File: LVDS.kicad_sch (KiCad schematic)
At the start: 16 parts, among them J13 DF13C-3P-1.25V_21_, J3 QSH-030-01-X-D-A-XX, U10 TCAN1042HVDQ1, U11 SN74AVC2T245_UQFN

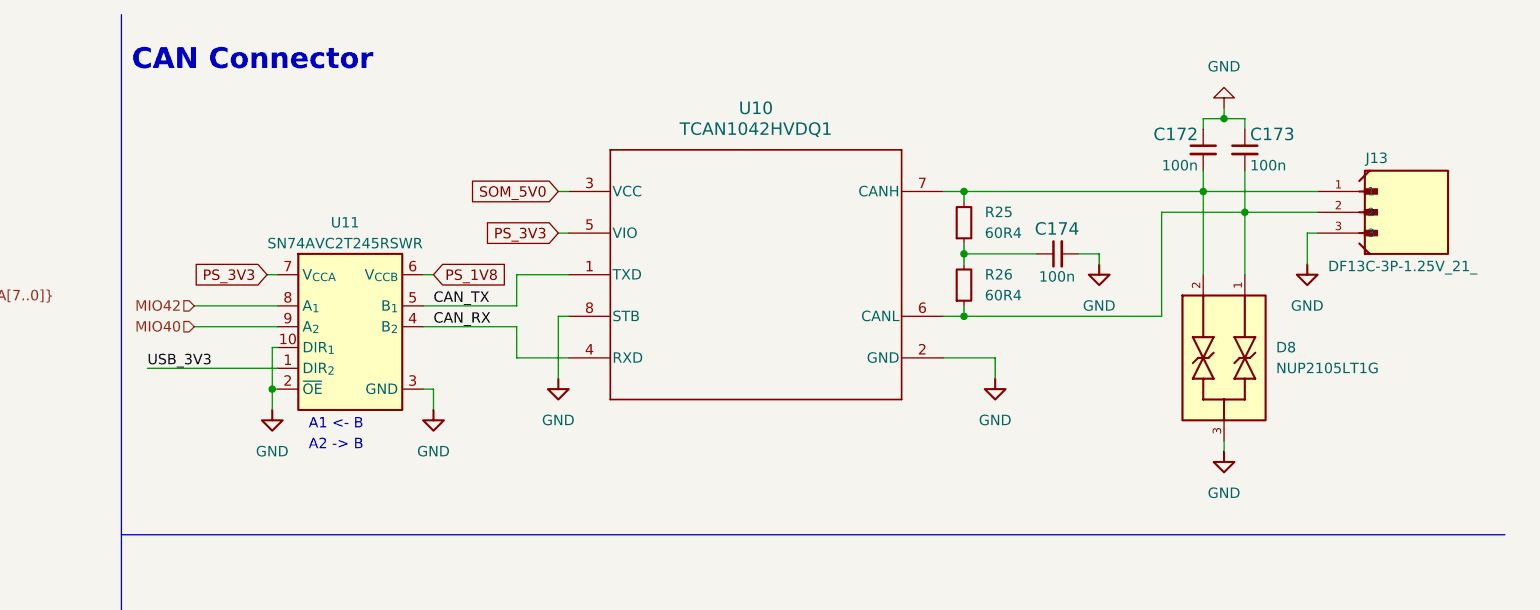
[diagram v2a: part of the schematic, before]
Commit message: Routed CAN portion of board
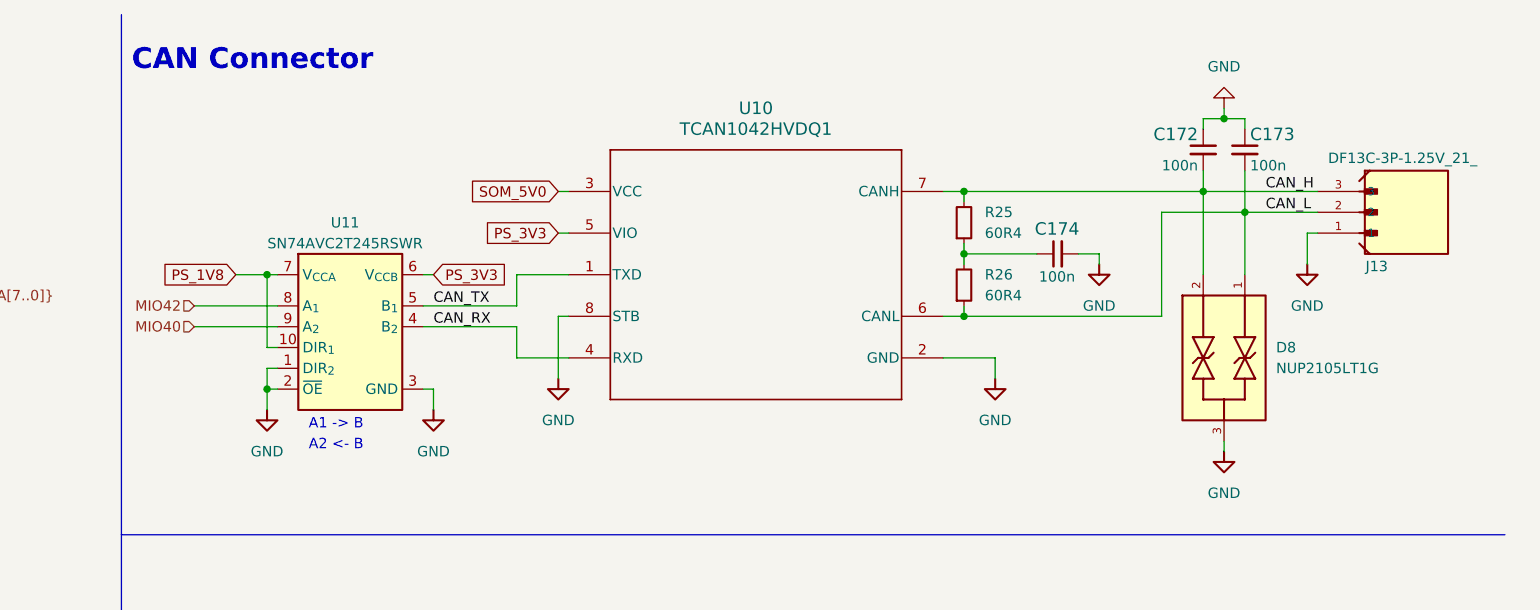
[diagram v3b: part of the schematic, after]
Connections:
- net USB_3V3 is gone; now on net GND: U11.1 (DIR_{2})
- net GND: now also J13.1; no longer J13.3, U11.10 (DIR_{1})
- net PS_1V8: now also U11.10 (DIR_{1}), U11.7 (V_{CCA}); no longer U11.6 (V_{CCB})
- net PS_3V3: now also U11.6 (V_{CCB}); no longer U11.7 (V_{CCA})
- net CAN_H: now reaches C172.2, D8.2, R25.2, U10.7 (CANH)
- net CAN_H: now also J13.3; no longer J13.1
- net CAN_L: now reaches C173.2, D8.1, J13.2, R26.1, U10.6 (CANL)
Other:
- note added: "A1 -> B"
- note added: "A2 <- B"
- note removed: "A1 <- B"
- note removed: "A2 -> B"
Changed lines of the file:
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@@
 		)
 	)
-	(text "A2 -> B"
+	(text "A2 <- B"
 		(exclude_from_sim no)
 		(at 138.43 66.04 0)
@@
 		)
 	)
-	(text "A1 <- B"
+	(text "A1 -> B"
 		(exclude_from_sim no)
 		(at 138.43 63.5 0)
@@
 	)
 	(junction
-		(at 218.44 41.91)
+		(at 133.35 44.45)
 		(diameter 0)
 		(color 0 0 0 0)
 	)
 	(junction
-		(at 54.61 55.88)
+		(at 218.44 41.91)
 		(diameter 0)
 		(color 0 0 0 0)
 	)
 	(junction
-		(at 218.44 34.29)
+		(at 54.61 55.88)
 		(diameter 0)
 		(color 0 0 0 0)
 	)
 	(junction
-		(at 133.985 58.42)
+		(at 218.44 34.29)
 		(diameter 0)
 		(color 0 0 0 0)
@@
 	)
 	(junction
+		(at 133.35 58.42)
+		(diameter 0)
+		(color 0 0 0 0)
+	)
+	(junction
 		(at 54.61 109.22)
 		(diameter 0)
@@
 	(wire
 		(pts
-			(xy 133.985 58.42) (xy 134.62 58.42)
+			(xy 133.35 58.42) (xy 134.62 58.42)
 		)
 		(stroke
@@
 	(wire
 		(pts
+			(xy 133.35 44.45) (xy 134.62 44.45)
+		)
+		(stroke
+			(width 0)
+			(type default)
+		)
+	)
+	(wire
+		(pts
 			(xy 152.4 44.45) (xy 153.67 44.45)
 		)
@@
 	(wire
 		(pts
-			(xy 53.34 55.88) (xy 54.61 55.88)
+			(xy 133.35 55.88) (xy 134.62 55.88)
 		)
 		(stroke
@@
 	(wire
 		(pts
-			(xy 234.95 43.18) (xy 234.95 41.91)
+			(xy 129.54 44.45) (xy 133.35 44.45)
 		)
 		(stroke
@@
 	(wire
 		(pts
-			(xy 168.91 39.37) (xy 170.18 39.37)
+			(xy 53.34 55.88) (xy 54.61 55.88)
 		)
 		(stroke
@@
 	(wire
 		(pts
-			(xy 54.61 71.12) (xy 54.61 78.74)
+			(xy 234.95 43.18) (xy 234.95 41.91)
 		)
 		(stroke
@@
 	(wire
 		(pts
-			(xy 53.34 58.42) (xy 91.44 58.42)
+			(xy 168.91 39.37) (xy 170.18 39.37)
 		)
 		(stroke
@@
 	(wire
 		(pts
-			(xy 134.62 53.34) (xy 133.985 53.34)
+			(xy 54.61 71.12) (xy 54.61 78.74)
+		)
+		(stroke
+			(width 0)
+			(type default)
+		)
+	)
+	(wire
+		(pts
+			(xy 53.34 58.42) (xy 91.44 58.42)
 		)
 		(stroke
@@
 	(wire
 		(pts
-			(xy 133.985 58.42) (xy 133.985 60.96)
+			(xy 133.35 58.42) (xy 133.35 60.96)
 		)
 		(stroke
@@
 	(wire
 		(pts
-			(xy 24.13 147.32) (xy 24.13 148.59)
+			(xy 133.35 55.88) (xy 133.35 58.42)
 		)
 		(stroke
@@
 	(wire
 		(pts
-			(xy 133.35 44.45) (xy 134.62 44.45)
+			(xy 24.13 147.32) (xy 24.13 148.59)
 		)
 		(stroke
@@
 	(wire
 		(pts
+			(xy 133.35 44.45) (xy 133.35 53.34)
+		)
+		(stroke
+			(width 0)
+			(type default)
+		)
+	)
+	(wire
+		(pts
 			(xy 168.91 49.53) (xy 168.91 57.15)
 		)
@@
 	(wire
 		(pts
-			(xy 134.62 55.88) (xy 118.745 55.88)
+			(xy 53.34 88.9) (xy 91.44 88.9)
 		)
 		(stroke
@@
 	(wire
 		(pts
-			(xy 53.34 88.9) (xy 91.44 88.9)
+			(xy 218.44 48.26) (xy 218.44 49.53)
 		)
 		(stroke
@@
 	(wire
 		(pts
-			(xy 218.44 48.26) (xy 218.44 49.53)
+			(xy 53.34 96.52) (xy 91.44 96.52)
 		)
 		(stroke
@@
 	(wire
 		(pts
-			(xy 53.34 96.52) (xy 91.44 96.52)
+			(xy 53.34 86.36) (xy 54.61 86.36)
 		)
 		(stroke
@@
 	(wire
 		(pts
-			(xy 53.34 86.36) (xy 54.61 86.36)
+			(xy 124.46 48.26) (xy 134.62 48.26)
 		)
 		(stroke
@@
 	(wire
 		(pts
-			(xy 124.46 48.26) (xy 134.62 48.26)
+			(xy 54.61 101.6) (xy 54.61 106.68)
 		)
 		(stroke
@@
 	(wire
 		(pts
-			(xy 54.61 101.6) (xy 54.61 106.68)
+			(xy 53.34 48.26) (xy 54.61 48.26)
 		)
 		(stroke
@@
 	(wire
 		(pts
-			(xy 53.34 48.26) (xy 54.61 48.26)
+			(xy 133.35 53.34) (xy 134.62 53.34)
 		)
 		(stroke
@@
 	(wire
 		(pts
-			(xy 133.985 53.34) (xy 133.985 58.42)
-		)
-		(stroke
-			(width 0)
-			(type default)
-		)
-	)
-	(wire
-		(pts
 			(xy 168.91 34.29) (xy 170.18 34.29)
 		)
@@
 		)
 	)
+	(label "CAN_L"
+		(at 255.27 36.83 0)
+		(effects
+			(font
+				(size 1.27 1.27)
+			)
+			(justify left bottom)
+		)
+	)
 	(label "HPA02_N"
 		(at 90.17 91.44 180)
@@
 		)
 	)
+	(label "CAN_H"
+		(at 255.27 34.29 0)
+		(effects
+			(font
+				(size 1.27 1.27)
+			)
+			(justify left bottom)
+		)
+	)
 	(label "HPA02_P"
 		(at 90.17 88.9 180)
@@
 		)
 	)
-	(label "USB_3V3"
-		(at 118.745 55.88 0)
-		(effects
-			(font
-				(size 1.27 1.27)
-			)
-			(justify left bottom)
-		)
-	)
 	(label "LVDS_2P"
 		(at 68.58 73.66 180)
@@
 	(global_label "PS_1V8"
 		(shape input)
-		(at 153.67 44.45 0)
+		(at 129.54 44.45 180)
 		(fields_autoplaced yes)
 		(effects
@@
 				(size 1.27 1.27)
 			)
-			(justify left)
+			(justify right)
 		)
 		(property "Intersheetrefs" "${INTERSHEET_REFS}"
-			(at 162.949 44.3706 0)
+			(at 120.261 44.3706 0)
 			(effects
 				(font
 					(size 1.27 1.27)
 				)
-				(justify left)
+				(justify right)
 				(hide yes)
 			)
@@
 	(global_label "PS_3V3"
 		(shape input)
-		(at 133.35 44.45 180)
+		(at 153.67 44.45 0)
 		(fields_autoplaced yes)
 		(effects
@@
 				(size 1.27 1.27)
 			)
-			(justify right)
+			(justify left)
 		)
 		(property "Intersheetrefs" "${INTERSHEET_REFS}"
-			(at 101.6 -204.47 0)
+			(at 185.42 -204.47 0)
 			(effects
 				(font
 					(size 1.27 1.27)
 				)
-				(justify left)
+				(justify right)
 				(hide yes)
 			)
@@
 		(lib_id "kria-k26-devboard:DF13C-3P-1.25V_21_")
 		(at 271.78 36.83 0)
+		(mirror x)
 		(unit 1)
 		(exclude_from_sim no)
@@
 		(dnp no)
 		(property "Reference" "J13"
-			(at 267.462 30.226 0)
+			(at 267.462 43.434 0)
 			(effects
 				(font
@@
 		)
 		(property "Value" "DF13C-3P-1.25V_21_"
-			(at 262.89 43.434 0)
+			(at 262.89 30.226 0)
 			(effects
 				(font
@@
 	(symbol
 		(lib_id "kria-k26-devboard:GND")
-		(at 133.985 60.96 0)
+		(at 133.35 60.96 0)
 		(unit 1)
 		(exclude_from_sim no)
@@
 		(fields_autoplaced yes)
 		(property "Reference" "#PWR018"
-			(at 133.985 67.31 0)
+			(at 133.35 67.31 0)
 			(effects
 				(font
@@
 		)
 		(property "Value" "GND"
-			(at 133.985 66.04 0)
+			(at 133.35 66.04 0)
 			(effects
 				(font
@@
 		)
 		(property "Footprint" ""
-			(at 142.875 68.58 0)
+			(at 142.24 68.58 0)
 			(effects
 				(font
@@
 		)
 		(property "Datasheet" ""
-			(at 142.875 73.66 0)
+			(at 142.24 73.66 0)
 			(effects
 				(font
@@
 		)
 		(property "Description" ""
-			(at 133.985 60.96 0)
+			(at 133.35 60.96 0)
 			(effects
 				(font
@@
 		)
 		(property "Author" "Antmicro"
-			(at 142.875 68.58 0)
+			(at 142.24 68.58 0)
 			(effects
 				(font
@@
 		)
 		(property "License" "Apache-2.0"
-			(at 142.875 71.12 0)
+			(at 142.24 71.12 0)
 			(effects
 				(font

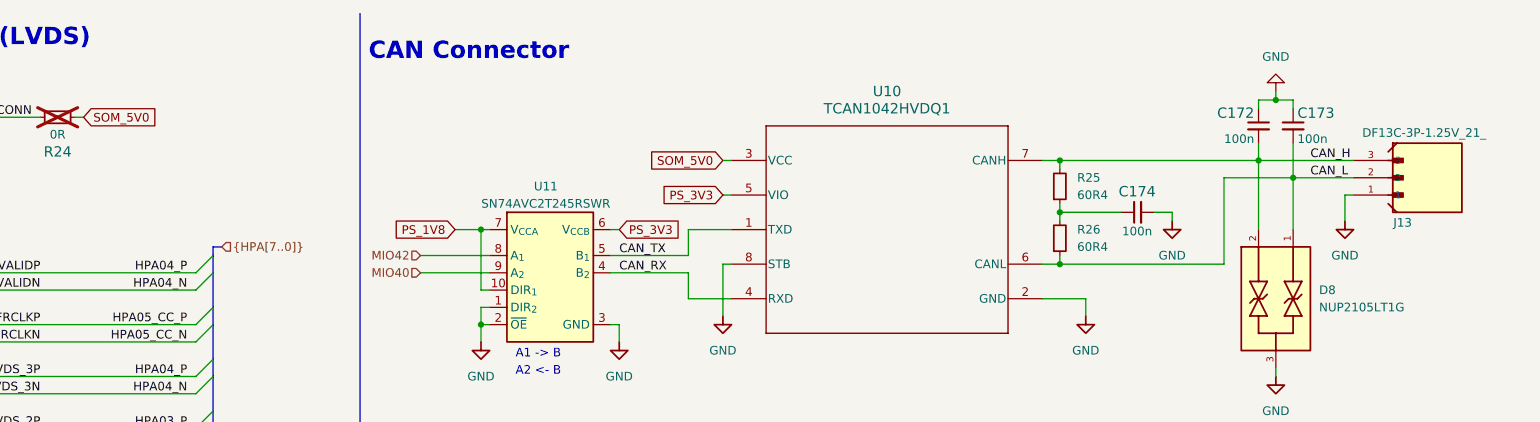
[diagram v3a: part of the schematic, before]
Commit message: Finished first set of LVDS signals
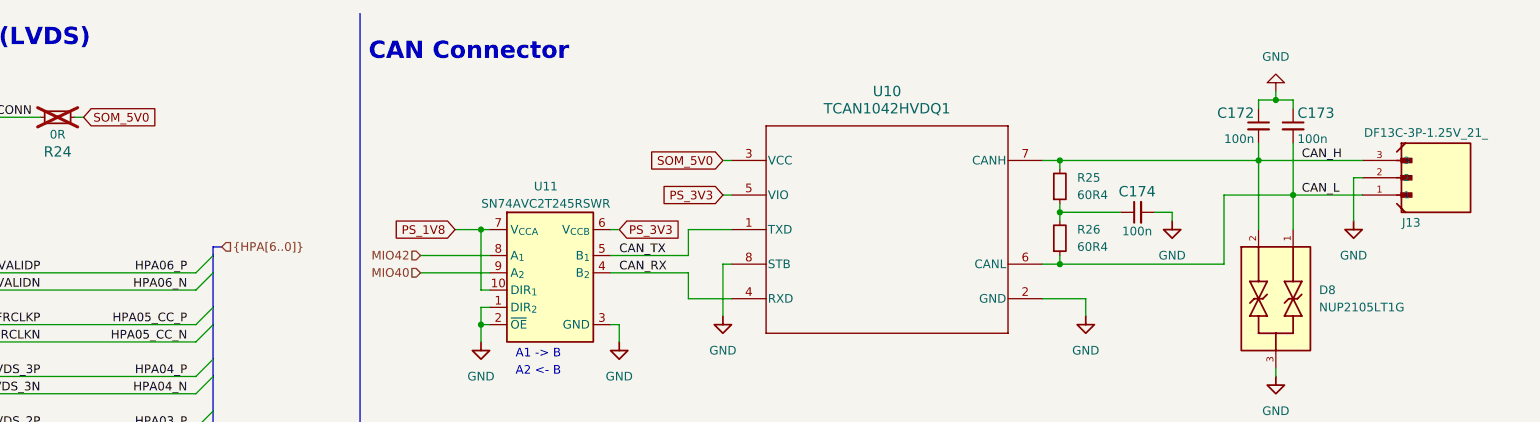
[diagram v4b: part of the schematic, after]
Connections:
- net CAN_L: now also J13.1; no longer J13.2
- net GND: now also J13.2; no longer J13.1
- net HPA04_N: no longer J3.22
- net HPA04_P: no longer J3.20
- new net HPA06_N: J3.22
- new net HPA06_P: J3.20
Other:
- moved on the sheet: J13
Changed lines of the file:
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@@
+	)
+	(junction
+		(at 252.73 39.37)
+		(diameter 0)
+		(color 0 0 0 0)
 	)
 	(junction
@@
 		(color 0 0 0 0)
 	)
-	(junction
-		(at 252.73 36.83)
-		(diameter 0)
-		(color 0 0 0 0)
-	)
 	(no_connect
 		(at 27.94 53.34)
@@
 	(wire
 		(pts
+			(xy 261.62 36.83) (xy 262.89 36.83)
+		)
+		(stroke
+			(width 0)
+			(type default)
+		)
+	)
+	(wire
+		(pts
 			(xy 53.34 68.58) (xy 91.44 68.58)
 		)
@@
 	(wire
 		(pts
-			(xy 247.65 34.29) (xy 261.62 34.29)
-		)
-		(stroke
-			(width 0)
-			(type default)
-		)
-	)
-	(wire
-		(pts
-			(xy 252.73 31.75) (xy 252.73 36.83)
+			(xy 247.65 34.29) (xy 262.89 34.29)
 		)
 		(stroke
@@
 		)
 	)
+	(wire
+		(pts
+			(xy 252.73 31.75) (xy 252.73 39.37)
+		)
+		(stroke
+			(width 0)
+			(type default)
+		)
+	)
 	(bus
 		(pts
@@
 	(wire
 		(pts
+			(xy 252.73 39.37) (xy 262.89 39.37)
+		)
+		(stroke
+			(width 0)
+			(type default)
+		)
+	)
+	(wire
+		(pts
 			(xy 54.61 55.88) (xy 54.61 63.5)
 		)
@@
 	(wire
 		(pts
-			(xy 252.73 36.83) (xy 261.62 36.83)
-		)
-		(stroke
-			(width 0)
-			(type default)
-		)
-	)
-	(wire
-		(pts
 			(xy 54.61 120.65) (xy 54.61 121.92)
 		)
@@
 	(wire
 		(pts
-			(xy 260.35 39.37) (xy 261.62 39.37)
-		)
-		(stroke
-			(width 0)
-			(type default)
-		)
-	)
-	(wire
-		(pts
 			(xy 133.35 55.88) (xy 133.35 58.42)
 		)
@@
 	(wire
 		(pts
-			(xy 252.73 36.83) (xy 252.73 44.45)
-		)
-		(stroke
-			(width 0)
-			(type default)
-		)
-	)
-	(wire
-		(pts
 			(xy 53.34 76.2) (xy 91.44 76.2)
 		)
@@
 	(wire
 		(pts
-			(xy 242.57 49.53) (xy 242.57 36.83)
+			(xy 242.57 49.53) (xy 242.57 39.37)
 		)
 		(stroke
@@
 	(wire
 		(pts
-			(xy 260.35 39.37) (xy 260.35 43.18)
-		)
-		(stroke
-			(width 0)
-			(type default)
-		)
-	)
-	(wire
-		(pts
 			(xy 24.13 140.97) (xy 22.86 140.97)
 		)
@@
 	(wire
 		(pts
+			(xy 252.73 39.37) (xy 252.73 44.45)
+		)
+		(stroke
+			(width 0)
+			(type default)
+		)
+	)
+	(wire
+		(pts
 			(xy 218.44 34.29) (xy 247.65 34.29)
 		)
@@
 	(wire
 		(pts
-			(xy 242.57 36.83) (xy 252.73 36.83)
+			(xy 242.57 39.37) (xy 252.73 39.37)
 		)
 		(stroke
@@
 		(pts
 			(xy 218.44 49.53) (xy 242.57 49.53)
+		)
+		(stroke
+			(width 0)
+			(type default)
+		)
+	)
+	(wire
+		(pts
+			(xy 261.62 36.83) (xy 261.62 43.18)
 		)
 		(stroke
@@
 	)
 	(label "CAN_L"
-		(at 255.27 36.83 0)
+		(at 254 39.37 0)
 		(effects
 			(font
@@
 		)
 	)
-	(label "HPA04_P"
+	(label "HPA06_P"
 		(at 90.17 50.8 180)
 		(effects
@@
 	)
 	(label "CAN_H"
-		(at 255.27 34.29 0)
+		(at 254 34.29 0)
 		(effects
 			(font
@@
 		)
 	)
-	(label "HPA04_N"
+	(label "HPA06_N"
 		(at 90.17 53.34 180)
 		(effects
@@
 		)
 	)
-	(hierarchical_label "{HPA[7..0]}"
+	(hierarchical_label "{HPA[6..0]}"
 		(shape input)
 		(at 95.25 46.99 0)
@@
 	(symbol
 		(lib_id "kria-k26-devboard:DF13C-3P-1.25V_21_")
-		(at 271.78 36.83 0)
+		(at 273.05 36.83 0)
 		(mirror x)
 		(unit 1)
@@
 		(dnp no)
 		(property "Reference" "J13"
-			(at 267.462 43.434 0)
+			(at 268.732 43.434 0)
 			(effects
 				(font
@@
 		)
 		(property "Value" "DF13C-3P-1.25V_21_"
-			(at 262.89 30.226 0)
+			(at 263.144 30.226 0)
 			(effects
 				(font
@@
 		)
 		(property "Footprint" "kria-k26-devboard-footprints:HRS_DF13C-3P-1.25V_21_"
-			(at 271.78 36.83 0)
+			(at 273.05 36.83 0)
 			(effects
 				(font
@@
 		)
 		(property "Datasheet" "https://www.hirose.com/product/series/catalogdownload?category=DF13"
-			(at 271.78 36.83 0)
+			(at 273.05 36.83 0)
 			(effects
 				(font
@@
 		)
 		(property "Description" "Connector Header Surface Mount 3 position 0.049\" (1.25mm)"
-			(at 271.78 36.83 0)
+			(at 273.05 36.83 0)
 			(effects
 				(font
@@
 		)
 		(property "MANUFACTURER" "HRS"
-			(at 271.78 36.83 0)
+			(at 273.05 36.83 0)
 			(effects
 				(font
@@
 	(symbol
 		(lib_id "kria-k26-devboard:GND")
-		(at 260.35 43.18 0)
+		(at 261.62 43.18 0)
 		(mirror y)
 		(unit 1)
@@
 		(fields_autoplaced yes)
 		(property "Reference" "#PWR051"
-			(at 260.35 49.53 0)
+			(at 261.62 49.53 0)
 			(effects
 				(font
@@
 		)
 		(property "Value" "GND"
-			(at 260.35 48.26 0)
+			(at 261.62 48.26 0)
 			(effects
 				(font
@@
 		)
 		(property "Footprint" ""
-			(at 251.46 50.8 0)
+			(at 252.73 50.8 0)
 			(effects
 				(font
@@
 		)
 		(property "Datasheet" ""
-			(at 251.46 55.88 0)
+			(at 252.73 55.88 0)
 			(effects
 				(font
@@
 		)
 		(property "Description" ""
-			(at 260.35 43.18 0)
+			(at 261.62 43.18 0)
 			(effects
 				(font
@@
 		)
 		(property "Author" "Antmicro"
-			(at 251.46 50.8 0)
+			(at 252.73 50.8 0)
 			(effects
 				(font
@@
 		)
 		(property "License" "Apache-2.0"
-			(at 251.46 53.34 0)
-			(effects
-				(font
+			(at 252.73 53.34 0)
+			(effects
+				(font

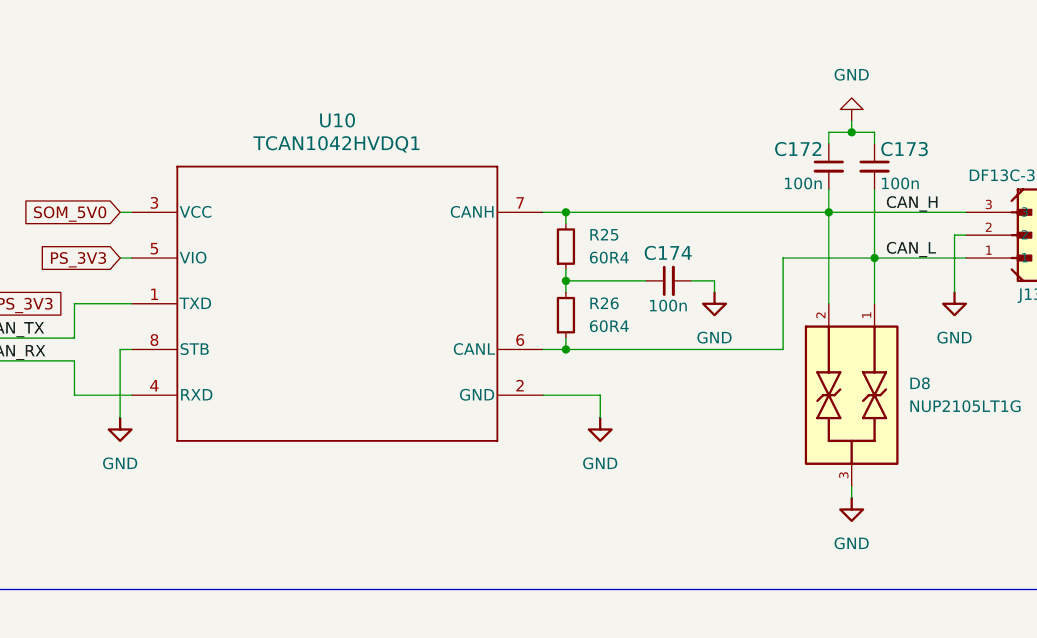
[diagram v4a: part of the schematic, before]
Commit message: Added shunts to CAN termination
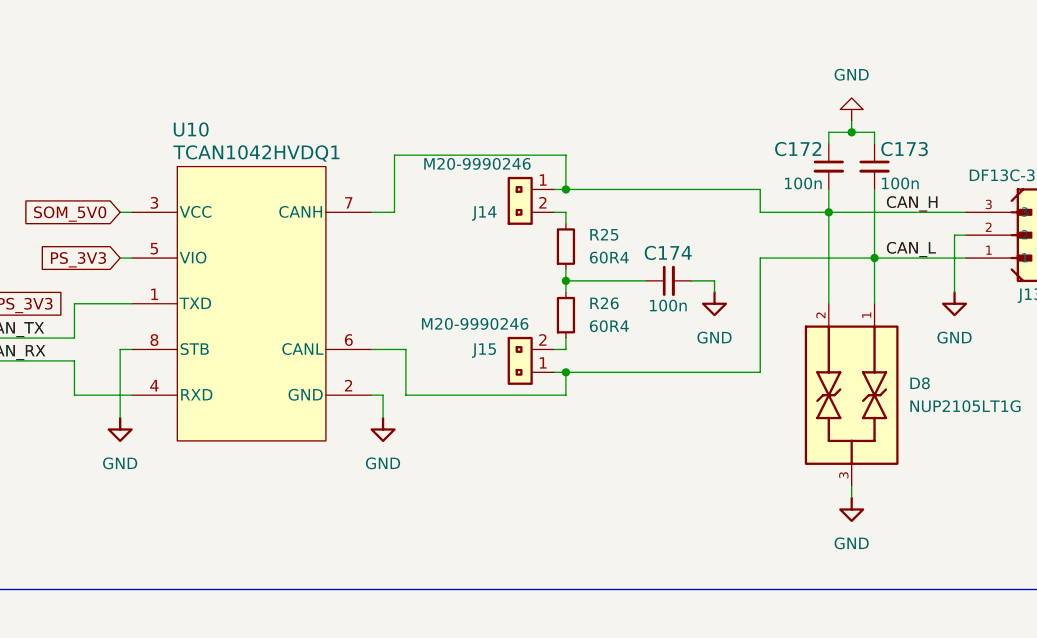
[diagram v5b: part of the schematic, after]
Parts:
- added J14, J15: PinHeader_1x2_P2.54mm_Drill1.02mm, kria-k26-devboard-footprints:PinHeader_1x2_P2.54mm_Drill1.02mm, symbol kria-k26-devboard:PinHeader_1x2_P2.54mm_Drill1.02mm
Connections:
- net CAN_H: now also J14.1; no longer R25.2
- net CAN_L: now also J15.1; no longer R26.1
- new net: J15.2, R26.1
- new net: J14.2, R25.2

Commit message: Added second radar board connector, but haven't routed LVDS lines yet
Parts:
- added J16: QSH-030-01-X-D-A-XX, kria-k26-devboard-footprints:SAMTEC-QTH-030-01-X-D-A, symbol kria-k26-devboard:QTH-030-01-X-D-A
- added R27, R28: R_0R_0402, kria-k26-devboard-footprints:R_0402_1005Metric, symbol kria-k26-devboard:R_0R_0402
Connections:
- net GND: now also R27.2
- net SOM_5V0: now also R28.2
- new net: J16.01, J16.02, J16.03, R28.1
- new net: J16.18, J16.24, J16.30, J16.36, J16.42, J16.48, J16.54, J16.60, J16.G1 (GND), J16.G2 (GND__1), J16.G3 (GND__2), J16.G4 (GND__3), R27.1
- new net HPC00_CC_N: J16.46
- new net HPC00_CC_P: J16.44
- new net HPC01_N: J16.58
- new net HPC01_P: J16.56
- new net HPC02_N: J16.52
- new net HPC02_P: J16.50
- new net HPC03_N: J16.40
- new net HPC03_P: J16.38
- new net HPC04_N: J16.34
- new net HPC04_P: J16.32
- new net HPC05_CC_N: J16.28
- new net HPC05_CC_P: J16.26
- new net HPC06_N: J16.22
- new net HPC06_P: J16.20
- no-connect marks 35 -> 70
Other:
- note added: "Radar Board Connector 1 (LVDS)"
- note added: "Radar Board Connector 2 (LVDS)"
- note removed: "Radar Board Connector (LVDS)"
- moved on the sheet: C172, C173, C174, D8, J13, J14, J15, R25, R26, U10, U11
